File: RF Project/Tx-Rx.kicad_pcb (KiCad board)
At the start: 2 copper layers, 30 x 55 mm, 26 parts, among them J1 CONN_Right, J2 CONN_Left, U1 CC2500RGPR, U2 U.FL_male

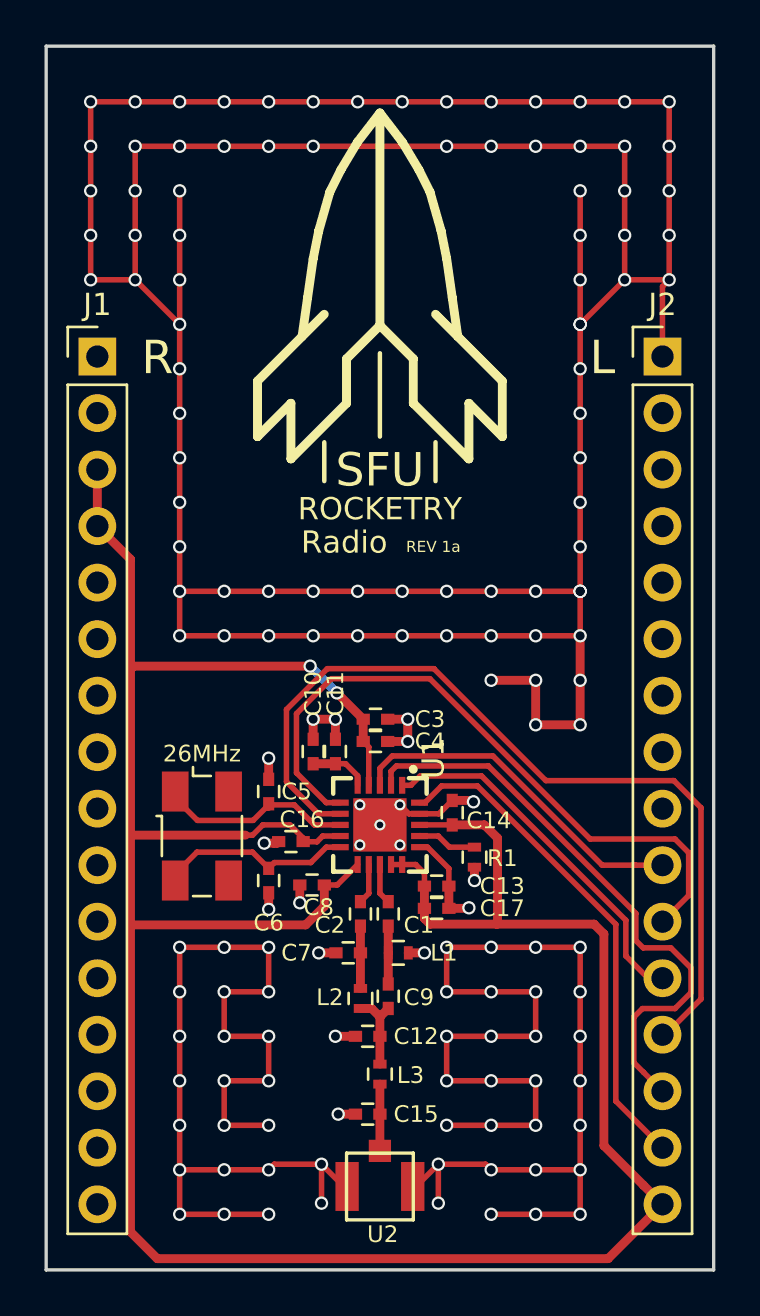
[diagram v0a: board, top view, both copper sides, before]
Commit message: Attempted to increase trace width to reduce impedance mismatch (could only achieve ~1mm or 88.3 Ohm vs the desired 50 Ohm), cleaned up some via placements/fills/silkscreen things
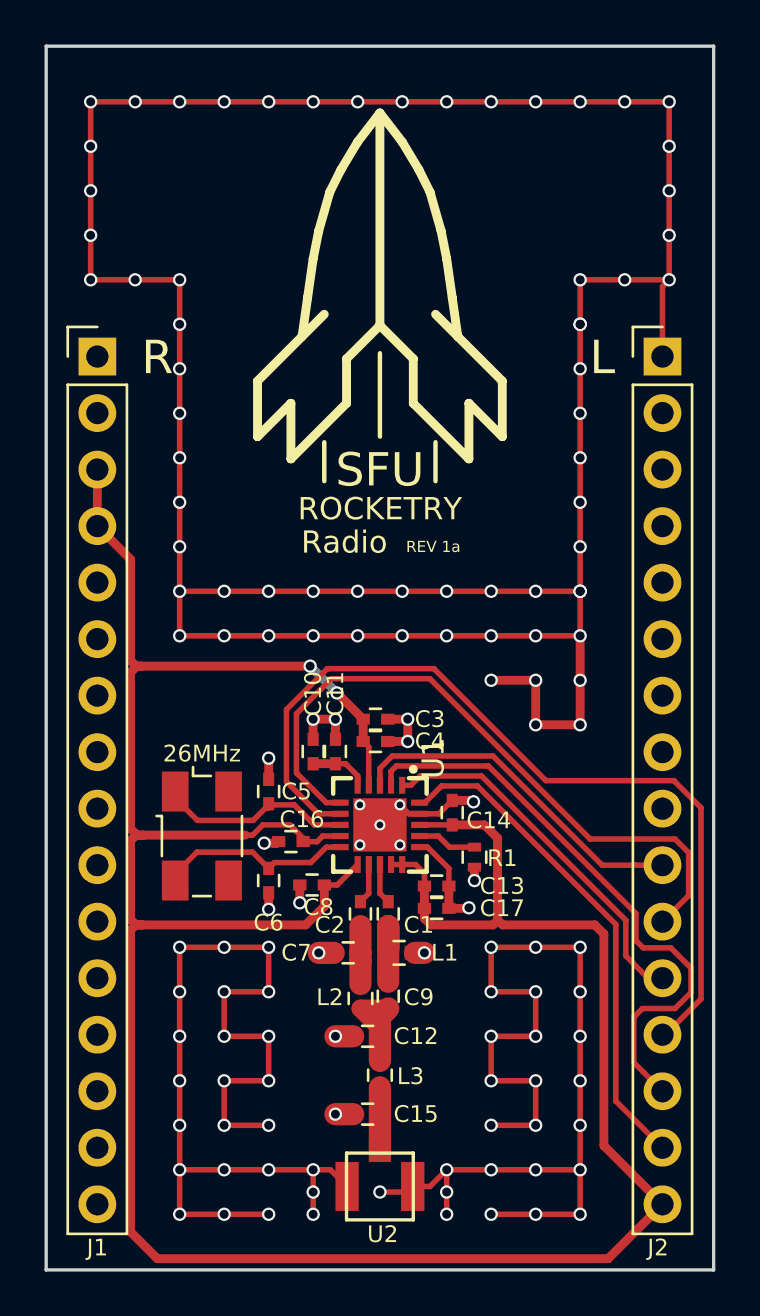
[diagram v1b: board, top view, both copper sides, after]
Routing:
- net PWR_GND: track 306.6 -> 254.1 mm, vias 154 -> 134
- net Net-(C12-Pad1): track 3.69 -> 6.57 mm
- net Net-(C15-Pad1): track 3.00 -> 4.15 mm
- net Net-(C1-Pad2): track 2.60 -> 3.52 mm
- net AVDD: track 130.0 -> 130.8 mm

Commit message: Exported GRBL files and final .zip
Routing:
- net (no net): track 0.00 -> 0.42 mm, vias 0 -> 1
- net PWR_GND: track 254.1 -> 253.7 mm, vias 134 -> 133
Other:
- rule pad_to_mask_clearance: 0.2 -> 0.05
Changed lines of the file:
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@@
   (general
     (links 70)
-    (no_connects 8)
-    (area 84.924999 72.424999 115.075001 127.575001)
+    (no_connects 10)
+    (area 64.650001 62.3 125.35 132.700001)
     (thickness 1.6)
     (drawings 93)
@@
     (pad_size 0.6 0.6)
     (pad_drill 0)
-    (pad_to_mask_clearance 0.2)
+    (pad_to_mask_clearance 0.05)
     (aux_axis_origin 0 0)
     (visible_elements 7FFFFFFF)
     (pcbplotparams
-      (layerselection 0x00030_80000001)
-      (usegerberextensions false)
+      (layerselection 0x010fc_80000001)
+      (usegerberextensions true)
       (excludeedgelayer true)
       (linewidth 0.100000)
@@
       (outputformat 1)
       (mirror false)
-      (drillshape 1)
+      (drillshape 0)
       (scaleselection 1)
-      (outputdirectory ""))
+      (outputdirectory Output/))
   )
   (net 0 "")
@@
   (gr_line (start 85 127.5) (end 115 127.5) (layer Edge.Cuts) (width 0.15))
   (gr_line (start 85 72.5) (end 85 127.5) (layer Edge.Cuts) (width 0.15))
+  (segment (start 102 113.25) (end 101.57501 113.25) (width 1) (layer F.Cu) (net 0))
+  (via (at 102 113.25) (size 0.6) (drill 0.4) (layers F.Cu B.Cu) (net 0))
   (segment (start 91.797071 107.297071) (end 90.8 106.3) (width 0.25) (layer F.Cu) (net 1))
   (segment (start 90.8 106.3) (end 90.8 106) (width 0.25) (layer F.Cu) (net 1))
@@
   (segment (start 98 117) (end 98.79999 117) (width 1) (layer F.Cu) (net 8))
   (segment (start 97.25 113.25) (end 97.92499 113.25) (width 1) (layer F.Cu) (net 8))
-  (segment (start 102 113.25) (end 101.57501 113.25) (width 1) (layer F.Cu) (net 8))
   (segment (start 100 124) (end 101.225 124) (width 0.25) (layer F.Cu) (net 8))
   (segment (start 101.225 124) (end 101.475 123.75) (width 0.25) (layer F.Cu) (net 8))
@@
   (segment (start 105 115) (end 105 113) (width 0.25) (layer F.Cu) (net 8))
   (segment (start 105 119) (end 105 117) (width 0.25) (layer F.Cu) (net 8))
-  (via (at 102 113.25) (size 0.6) (drill 0.4) (layers F.Cu B.Cu) (net 8))
   (via (at 98 120.5) (size 0.6) (drill 0.4) (layers F.Cu B.Cu) (net 8))
   (segment (start 109 103) (end 107 103) (width 0.4) (layer F.Cu) (net 8))

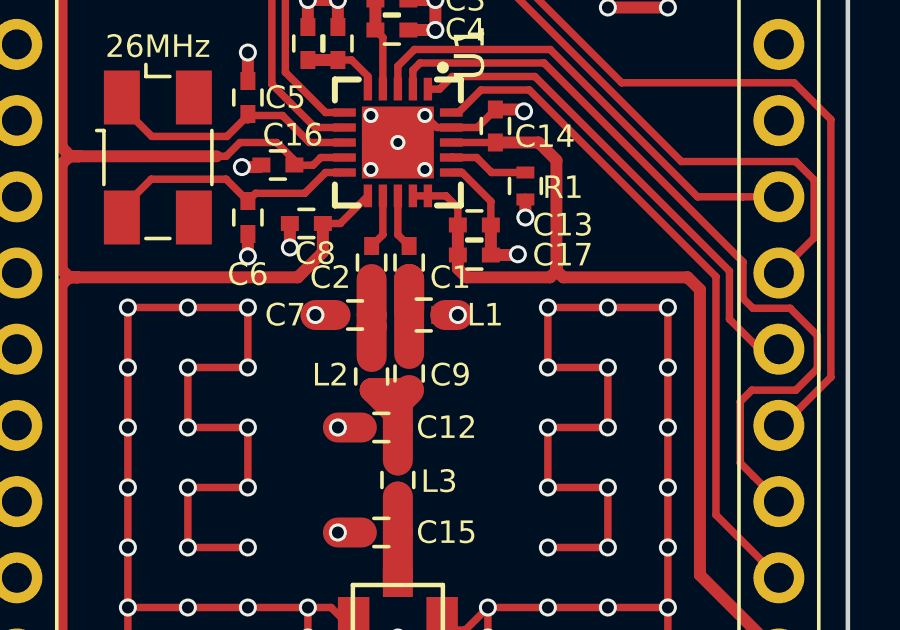
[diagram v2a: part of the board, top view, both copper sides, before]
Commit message: Fixed disconnection of a via on L1 of the RF output with the GND plane
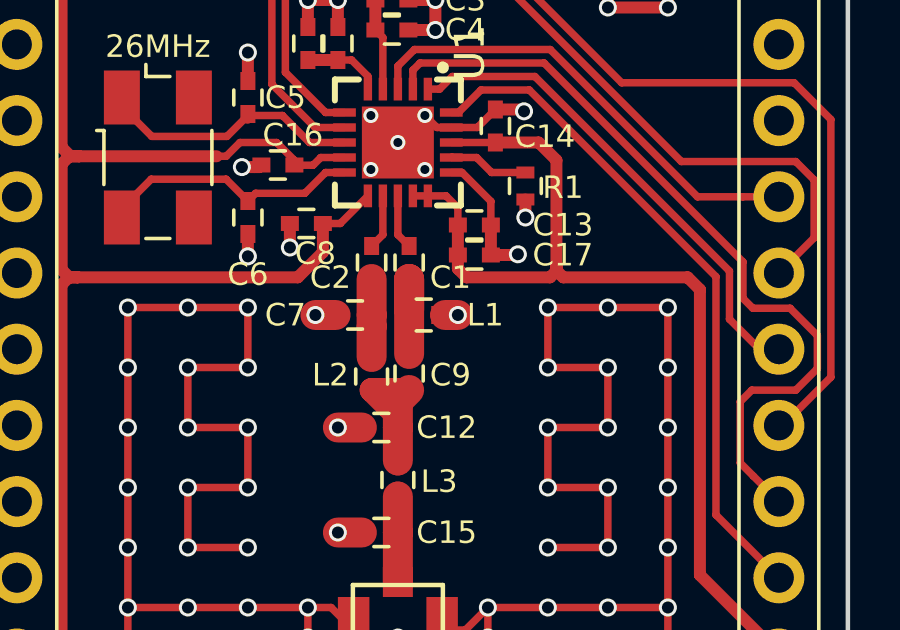
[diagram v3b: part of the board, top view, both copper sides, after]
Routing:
- net PWR_GND: track 253.7 -> 255.3 mm, vias 133 -> 134
- net (no net): track 0.42 -> 0.00 mm, vias 1 -> 0
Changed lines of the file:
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@@
     (area 64.650001 62.3 125.35 132.700001)
     (thickness 1.6)
-    (drawings 93)
-    (tracks 453)
+    (drawings 94)
+    (tracks 455)
     (zones 0)
     (modules 26)
@@
     (38 B.Mask user)
     (39 F.Mask user)
-    (40 Dwgs.User user hide)
+    (40 Dwgs.User user)
     (41 Cmts.User user)
     (42 Eco1.User user)
@@
       (net 8 PWR_GND))
   )
+  (dimension 20 (width 0.3) (layer Dwgs.User)
+    (gr_text "20.000 mm" (at 127.35 112 270) (layer Dwgs.User)
+      (effects (font (size 1.5 1.5) (thickness 0.3)))
+    )
+    (feature1 (pts (xy 121 122) (xy 128.7 122)))
+    (feature2 (pts (xy 121 102) (xy 128.7 102)))
+    (crossbar (pts (xy 126 102) (xy 126 122)))
+    (arrow1a (pts (xy 126 122) (xy 125.413579 120.873496)))
+    (arrow1b (pts (xy 126 122) (xy 126.586421 120.873496)))
+    (arrow2a (pts (xy 126 102) (xy 125.413579 103.126504)))
+    (arrow2b (pts (xy 126 102) (xy 126.586421 103.126504)))
+  )
   (gr_line (start 99 76.8) (end 100 75.5) (layer B.SilkS) (width 0.4))
   (gr_line (start 101 76.8) (end 100 75.5) (layer B.SilkS) (width 0.4))
@@
   (gr_line (start 85 127.5) (end 115 127.5) (layer Edge.Cuts) (width 0.15))
   (gr_line (start 85 72.5) (end 85 127.5) (layer Edge.Cuts) (width 0.15))
-  (segment (start 102 113.25) (end 101.57501 113.25) (width 1) (layer F.Cu) (net 0))
-  (via (at 102 113.25) (size 0.6) (drill 0.4) (layers F.Cu B.Cu) (net 0))
   (segment (start 91.797071 107.297071) (end 90.8 106.3) (width 0.25) (layer F.Cu) (net 1))
   (segment (start 90.8 106.3) (end 90.8 106) (width 0.25) (layer F.Cu) (net 1))
@@
   (segment (start 99.25 103.75) (end 99.5 104) (width 0.25) (layer F.Cu) (net 7))
   (segment (start 99.5 104) (end 99.5 105.72) (width 0.25) (layer F.Cu) (net 7))
+  (segment (start 102 113.25) (end 101.57501 113.25) (width 1) (layer F.Cu) (net 8))
+  (segment (start 102 113.25) (end 101.47501 113.25) (width 0.8) (layer F.Cu) (net 8))
+  (segment (start 101.311805 113.25) (end 102 113.25) (width 0.25) (layer F.Cu) (net 8))
+  (via (at 102 113.25) (size 0.6) (drill 0.4) (layers F.Cu B.Cu) (net 8))
   (segment (start 111 83) (end 109 83) (width 0.25) (layer F.Cu) (net 8))
   (segment (start 89 83) (end 91 83) (width 0.25) (layer F.Cu) (net 8))

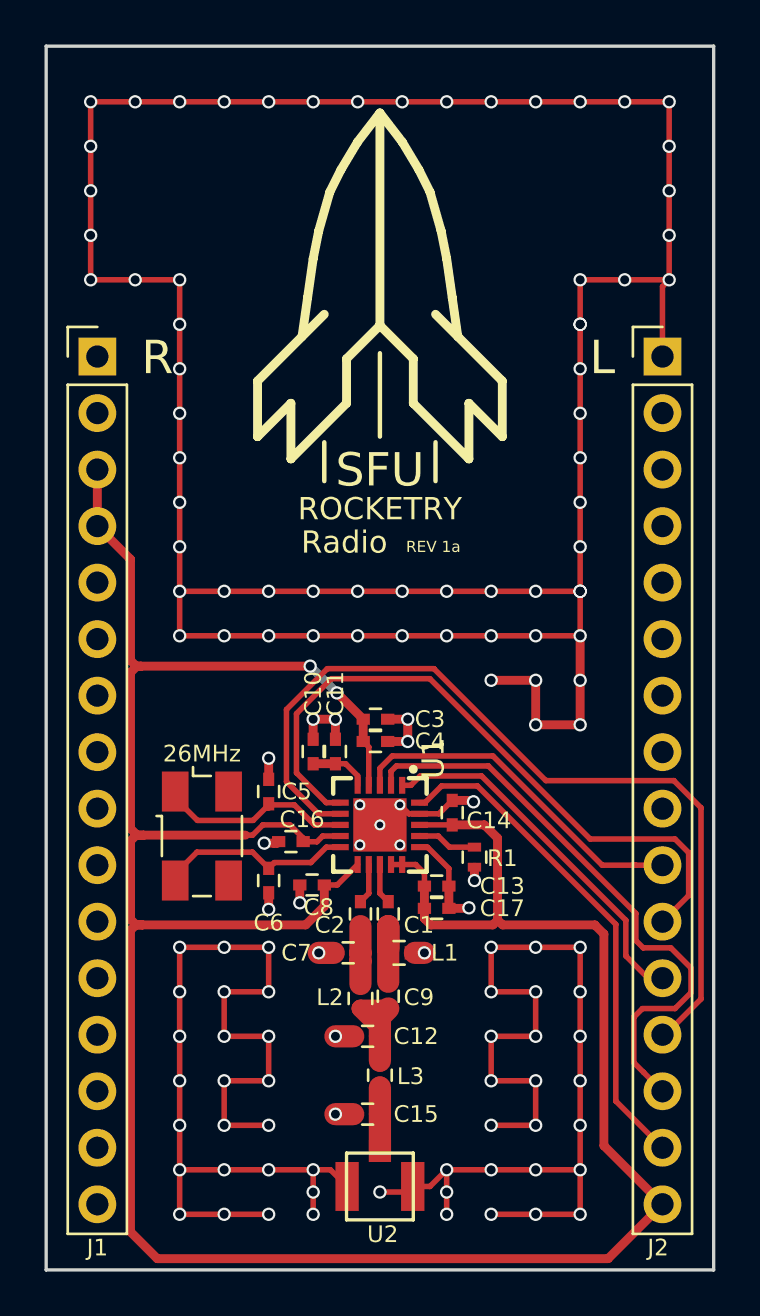
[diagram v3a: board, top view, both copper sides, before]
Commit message: Layout Revision 1b complete, notable additions: 1) Moved headers onto correct side, added pads for a RF Shield, main feed line to UFL connector is impedance matched to ~50ohm, incrememted the revision number from 1a to 1b (yay) and added some easter eggs
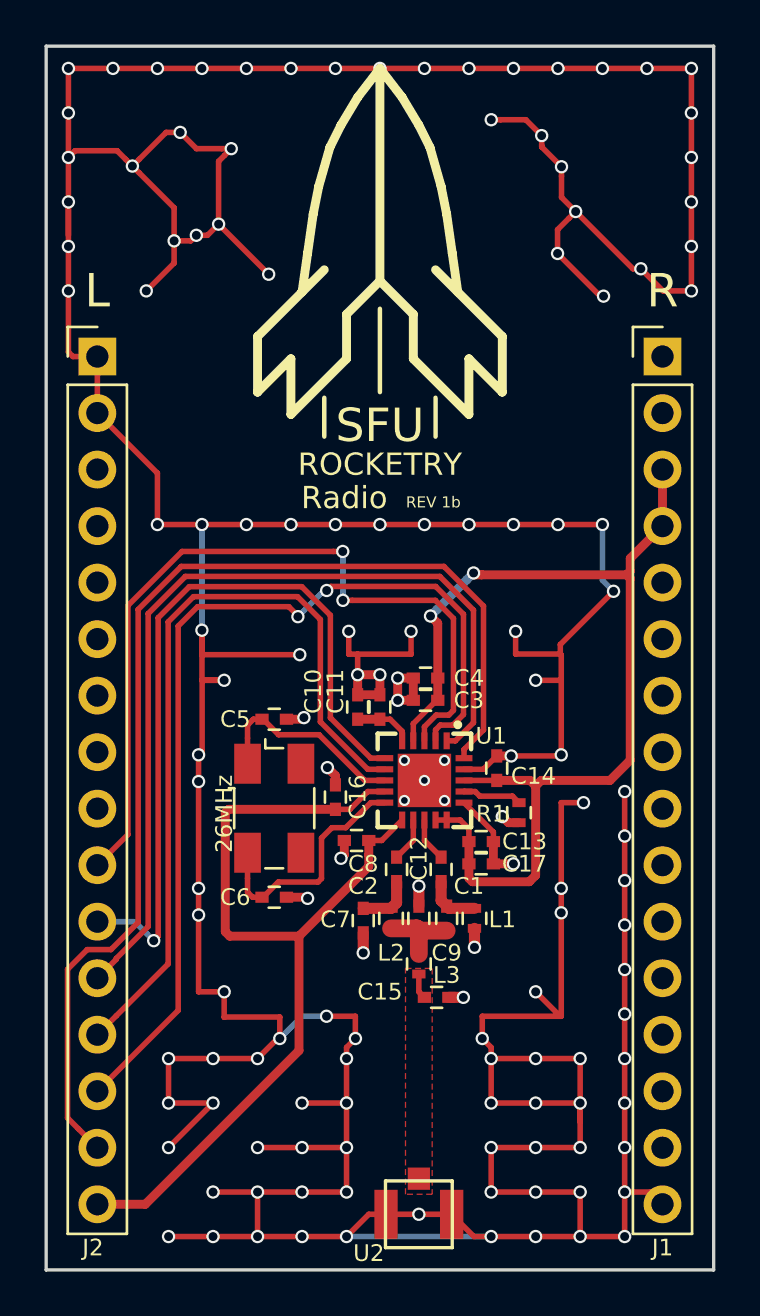
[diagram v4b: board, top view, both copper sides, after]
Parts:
- moved J1 25.4 mm to (112.7, 86.5)
- moved J2 25.4 mm to (87.3, 86.5)
- moved C15 6.10 mm to (102.5, 115.2), turned to 0 degrees
- moved C12 5.78 mm to (101.8, 111.7), turned to 90 degrees
- moved L3 5.30 mm to (101.8, 113.8)
- moved C9 4.38 mm to (103.0, 111.7)
- moved L2 3.85 mm to (100.5, 111.7)
- moved L1 3.73 mm to (104.2, 111.7), turned to 270 degrees
- moved C4 3.63 mm to (102.0, 100.9), turned to 180 degrees
- moved 26Mhtz1 3.48 mm to (95.2, 106.8)
- moved C5 3.26 mm to (95.2, 102.8), turned to 0 degrees
- moved C1 3.10 mm to (102.8, 109.5)
- moved C10 2.83 mm to (99.0, 102.2)
- moved C11 2.83 mm to (100.0, 102.2)
- moved C13 2.83 mm to (104.5, 108.2)
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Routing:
- net PWR_GND: track 255.3 -> 350.1 mm, vias 134 -> 141
- net AVDD: track 130.8 -> 89.8 mm
- net PD3/SI: track 22.6 -> 50.9 mm
- net PD0/SCLK: track 16.6 -> 39.9 mm
- net PE4/GD02: track 15.7 -> 36.8 mm, vias 0 -> 2
- net PD2/SO(GDO1): track 26.7 -> 43.4 mm, vias 0 -> 2
- net PE5/GDO0: track 30.3 -> 34.1 mm, vias 0 -> 1
- net PD1/CSn: track 39.2 -> 36.0 mm
- net Net-(C15-Pad1): track 4.15 -> 1.15 mm
- net Net-(C12-Pad1): track 6.57 -> 3.59 mm
- net XOSC_Q2: track 8.82 -> 11.2 mm
- net Net-(C1-Pad2): track 3.52 -> 2.49 mm
- net XOSC_Q1: track 8.87 -> 9.46 mm
- added copper zone on F.Cu, net Net-(C15-Pad1)
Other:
- rule pad_to_mask_clearance: 0.05 -> 0
- board text added: "REV 1b"
- board text removed: "REV 1a"

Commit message: GPS schematic and pcb track routing
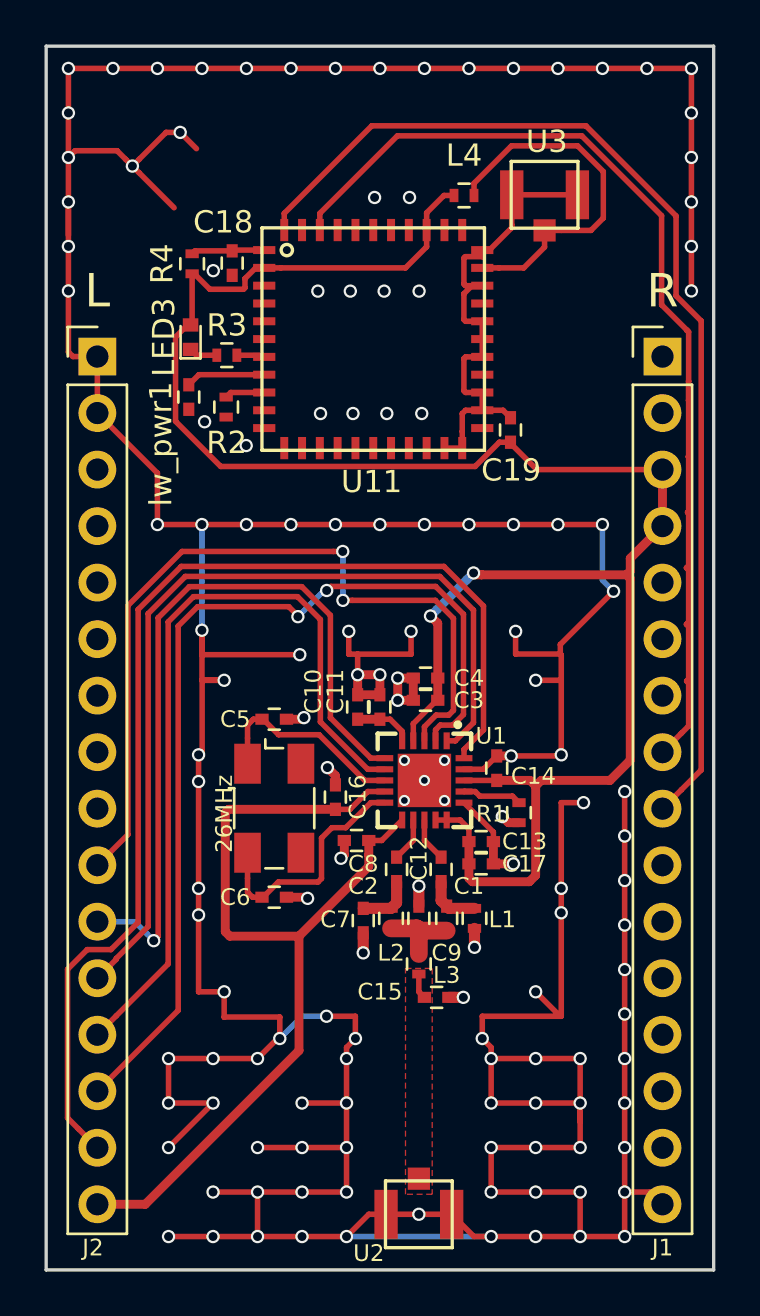
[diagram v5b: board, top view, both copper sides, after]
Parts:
- added C18: 1uF, Capacitors_SMD:C_0402, F.Cu at (93.4, 82.2)
- added C19: 22pF, Capacitors_SMD:C_0402, F.Cu at (105.9, 89.8)
- added L4: 33nH, Inductors_SMD:L_0402, F.Cu at (103.8, 79.2)
- added LED3: Green, LEDs:LED_0402, F.Cu at (91.5, 85.6)
- added R2: 10k, Resistors_SMD:R_0402, F.Cu at (93.1, 88.7)
- added R3: 330, Resistors_SMD:R_0402, F.Cu at (93.1, 86.4)
- added R4: 33k, Resistors_SMD:R_0402, F.Cu at (91.6, 82.3)
- added U11: Venus634SMD, RF_Transciever:VENUS634FLPX, F.Cu at (94.8, 81.7)
- added U3: U.FL_male, RF_Transciever:u.fl_male, F.Cu at (107.4, 79.2)
- added lw_pwr1: DNP, Capacitors_SMD:C_0402, F.Cu at (91.4, 88.3)
- R1: value 50 kOhm -> 56.2 kOhm
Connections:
- J1 pad 8: Net-(J1-Pad8) -> RX
- J1 pad 9: Net-(J1-Pad9) -> TX
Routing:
- net TX: track 0.00 -> 49.5 mm
- net AVDD: track 89.8 -> 136.1 mm
- net RX: track 0.00 -> 44.5 mm
- net PWR_GND: track 350.1 -> 316.8 mm
- net RF_GND: track 0.00 -> 22.6 mm
- net /GPS/RFIN: track 0.00 -> 16.4 mm
- net GPIO24: track 0.00 -> 3.58 mm
- net /GPS/RSTN: track 0.00 -> 3.31 mm
- net /GPS/BTSEL: track 0.00 -> 1.79 mm
- net Net-(LED3-Pad1): track 0.00 -> 1.29 mm
- net NAV: track 0.00 -> 1.26 mm
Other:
- board text removed: "ROCKETRY"
- board text removed: "SFU"
